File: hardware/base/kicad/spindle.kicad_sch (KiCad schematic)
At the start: 32 parts, among them J11 SPINDLE A, J12 SPINDLE B, Q5 SS8550, Q6 AO3422, Q7 AO3422, U36 OPA2990IDR, U37 SN74AHCT1G125DBVR

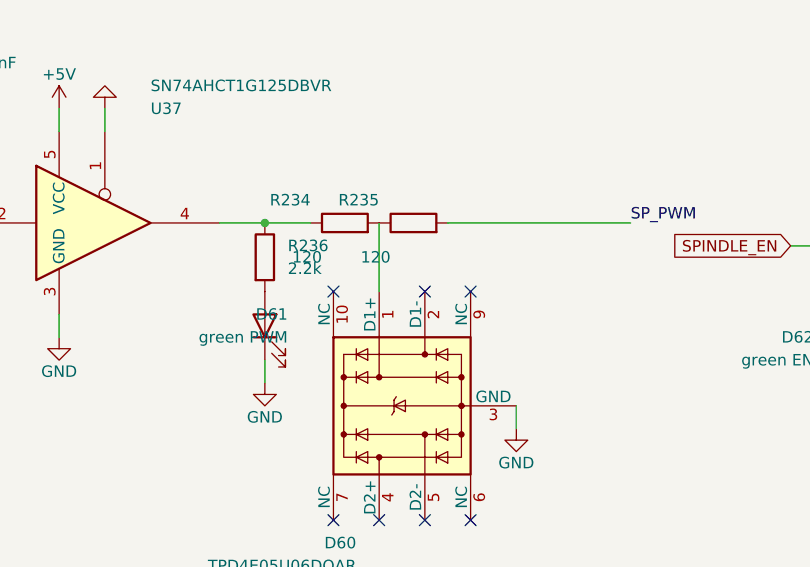
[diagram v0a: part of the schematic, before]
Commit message: Flow-through ESD arrays: the NC pin opposite each protected line carries it on every TPD4E05, not only on the PHY lines
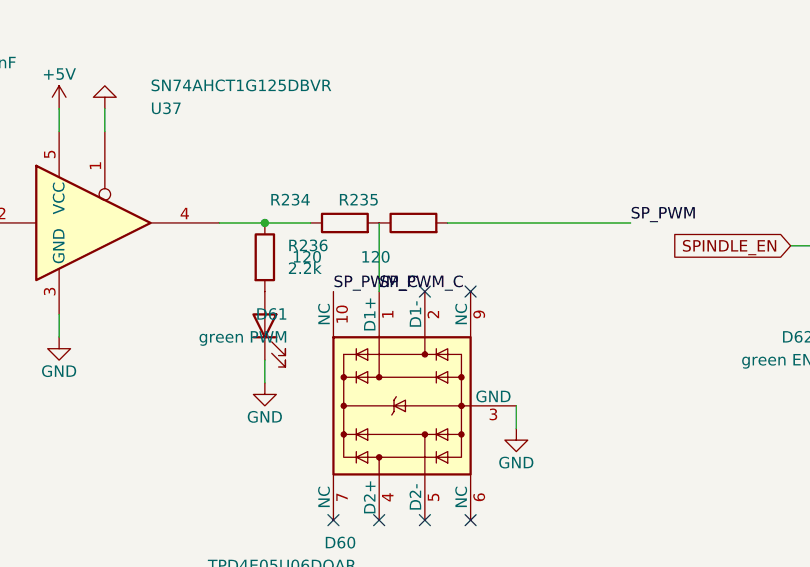
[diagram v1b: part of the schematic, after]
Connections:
- net SP_PWM_C: now reaches D60.1 (D1+), R234.2, R235.1
- net SP_PWM_C: now also D60.10 (NC)
- no-connect marks 8 -> 7
